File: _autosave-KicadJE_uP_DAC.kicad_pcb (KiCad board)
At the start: 2 copper layers, 100 x 100 mm, 275 parts, among them J201 CV1, J202 CV2, J203 OUT1, J204 OUT2, J205 IN1, J206 IN2, J301 AVR-ISP-6, J302 UART, J401 CV1, J402 CV2, J403 OUT1, J404 OUT2, J405 OUT3, J406 OUT4, J407 IN1, J408 IN2, J409 I2C, J501 BOOT, J502 UART, J503 USB_B_Micro, J601 CV1, J602 FM_lin, J603 Sync, J604 PWM, J605 Ramp, J606 Tri, J608 555_Pulse, P201 Doepfer_Power_16pin, P401 Doepfer_Power_16pin, P601 Doepfer_Power_10pin, Q601 MMBT2222A, SW201 SW_SPDT, SW401 SW_SPDT, U201 TL072, U202 MCP4822, U301 ATmega32A-AU, U401 TL072, U402 TL072, U405 MCP4822, U501 AMS1117-3.3, U502 STM32F103C8Tx, U601 TLC555, U602 TL074, U603 TL074, Y301 16MHz, Y501 8 MHz

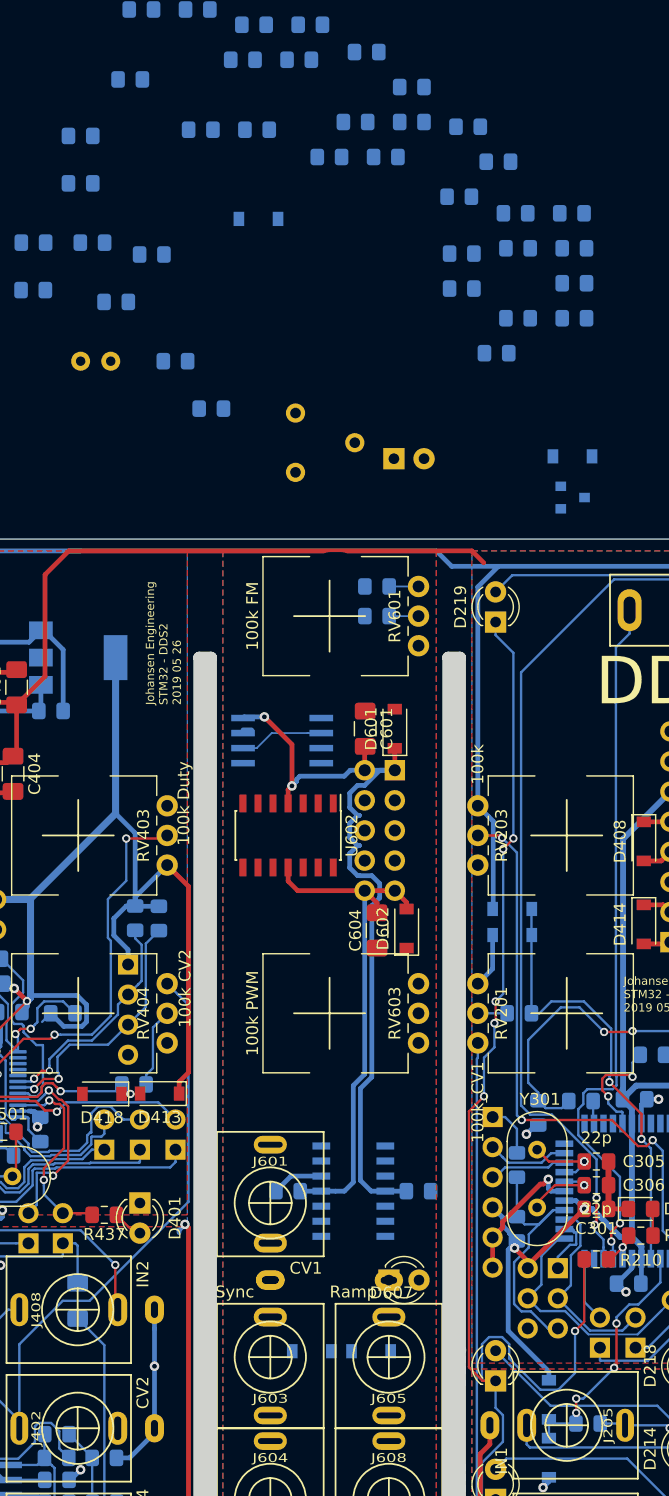
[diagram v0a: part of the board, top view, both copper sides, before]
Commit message: Labels mixup
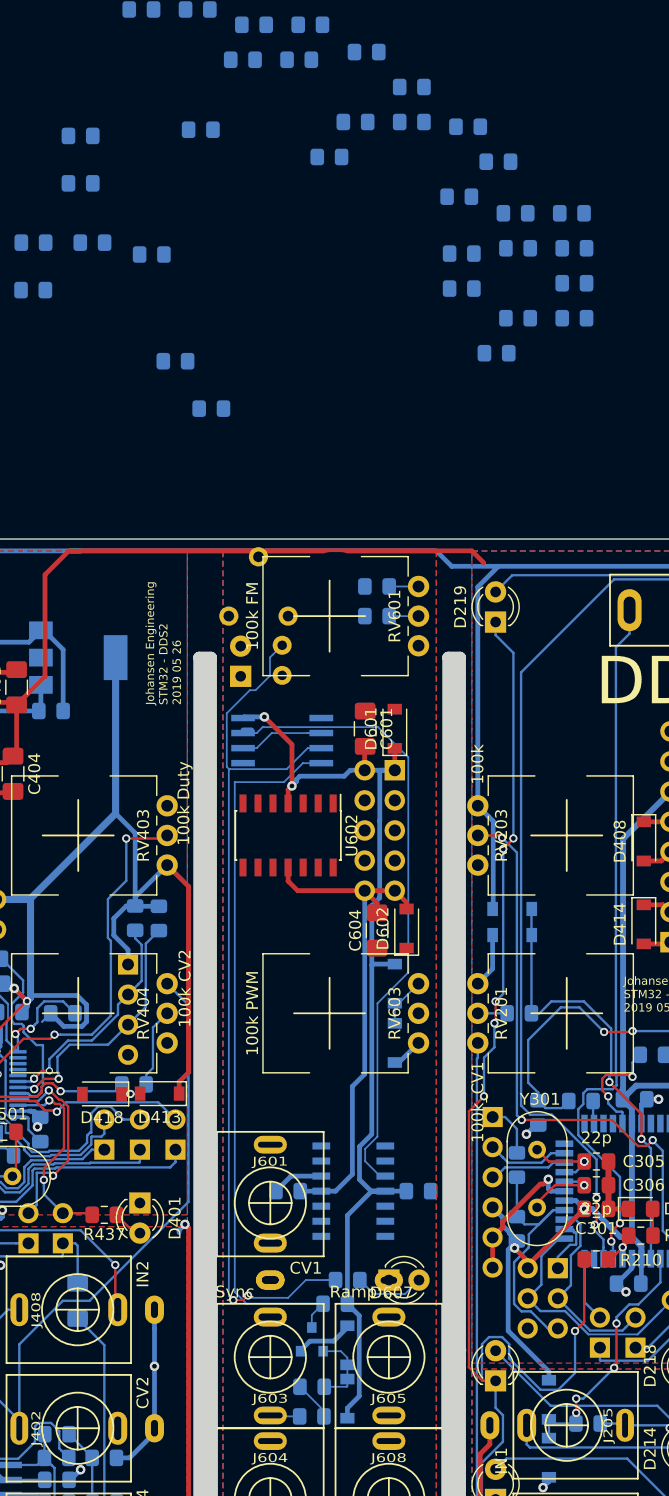
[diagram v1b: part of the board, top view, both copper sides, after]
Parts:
- moved C610 113.8 mm to (98.5, 124.0), turned to 180 degrees
- moved R618 103.9 mm to (98.5, 121.5)
- moved R601 99.2 mm to (100.5, 114.5)
- moved D604 95.3 mm to (101.5, 118.0), turned to 90 degrees
- moved R624 84.8 mm to (101.5, 112.5), turned to 180 degrees
- moved D603 81.7 mm to (101.5, 122.5), turned to 90 degrees
- moved Q601 74.3 mm to (98.5, 117.5), turned to 90 degrees
- moved D605 31.8 mm to (105.5, 87.5), turned to 270 degrees
- moved R607 31.5 mm to (96.0, 61.5), turned to 90 degrees
- moved D606 26.1 mm to (105.5, 92.5), turned to 270 degrees
- moved D611 22.4 mm to (92.5, 61.6), turned to 90 degrees
- moved RV602 18.0 mm to (91.5, 56.5), turned to 90 degrees
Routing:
- net 555_Out: track 0.00 -> 75.7 mm, vias 0 -> 2
- net Net-(Q601-Pad3): track 0.00 -> 61.2 mm
- net 555_Dis: track 0.72 -> 53.7 mm
- net +12V: track 263.4 -> 282.6 mm
- net GND: track 332.1 -> 339.7 mm
- net 555_Sync: track 0.00 -> 6.65 mm
- net Net-(D607-Pad2): track 0.00 -> 5.96 mm
- net 555_PWM: track 0.00 -> 4.38 mm
- net Net-(C610-Pad1): track 0.00 -> 3.34 mm
- net Net-(C610-Pad2): track 0.00 -> 2.51 mm
